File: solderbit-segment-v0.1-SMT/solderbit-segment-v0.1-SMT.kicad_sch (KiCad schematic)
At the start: 13 parts, among them J1 Conn_01x05_Pin, U1 PCF8574AT, U2 PCF8574N

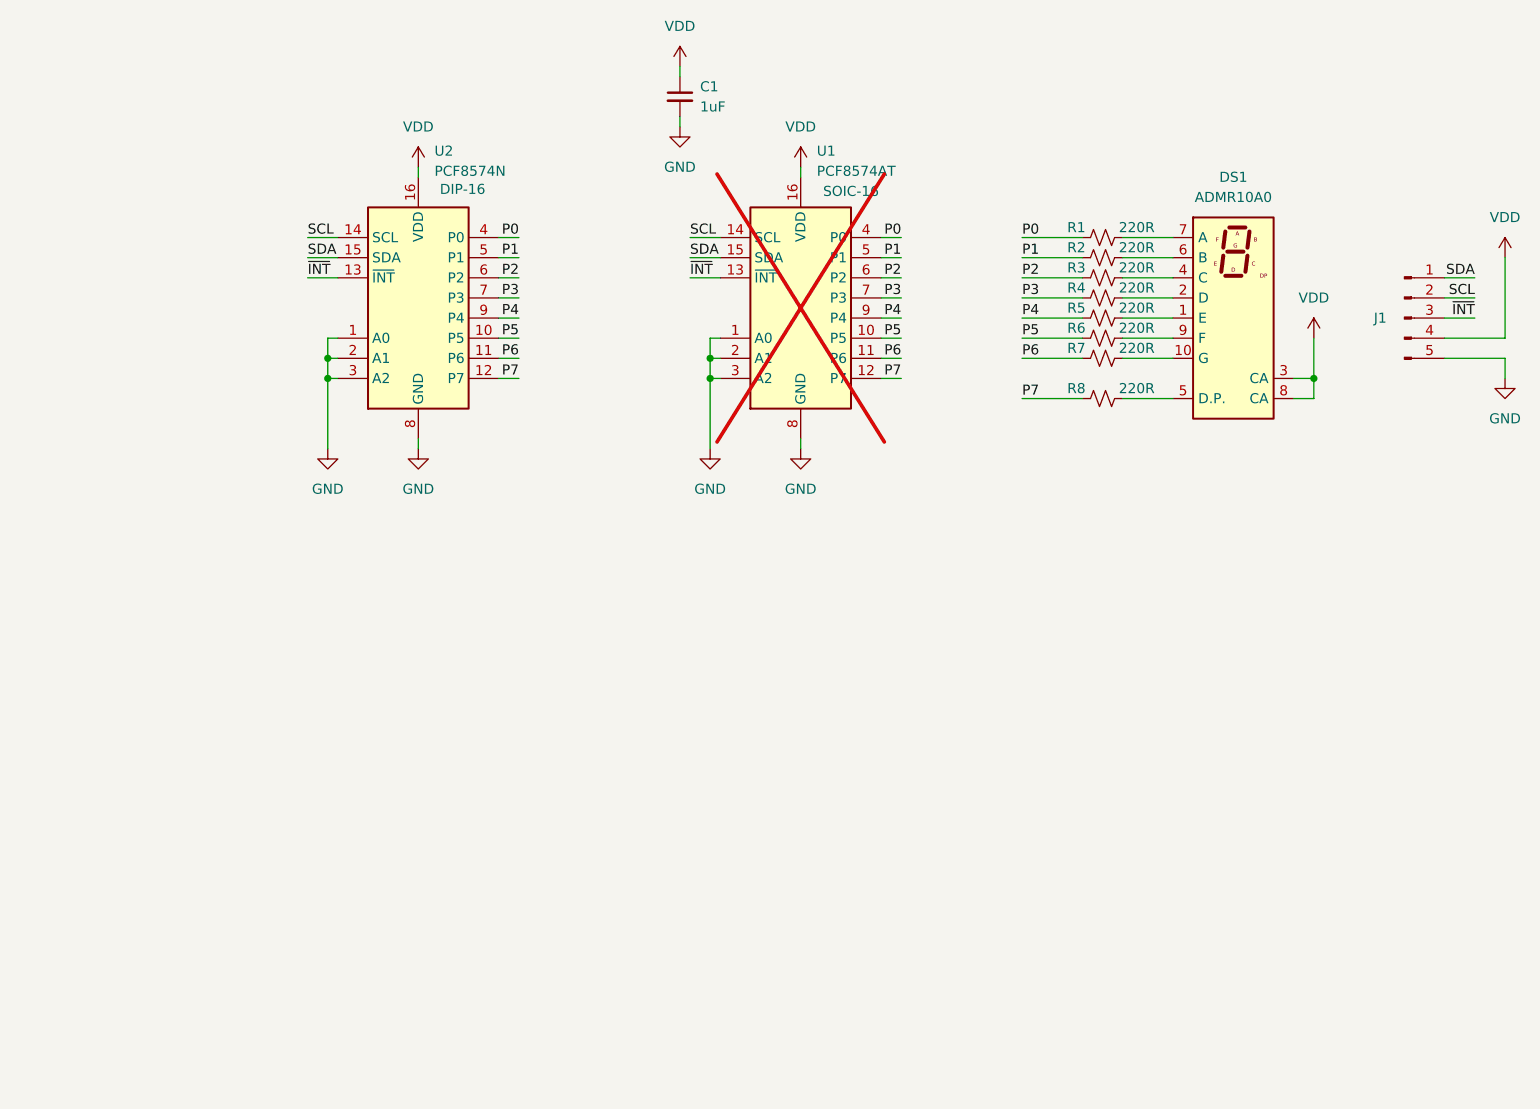
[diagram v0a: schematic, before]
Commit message: Separate SMT version, and THT I/O expander
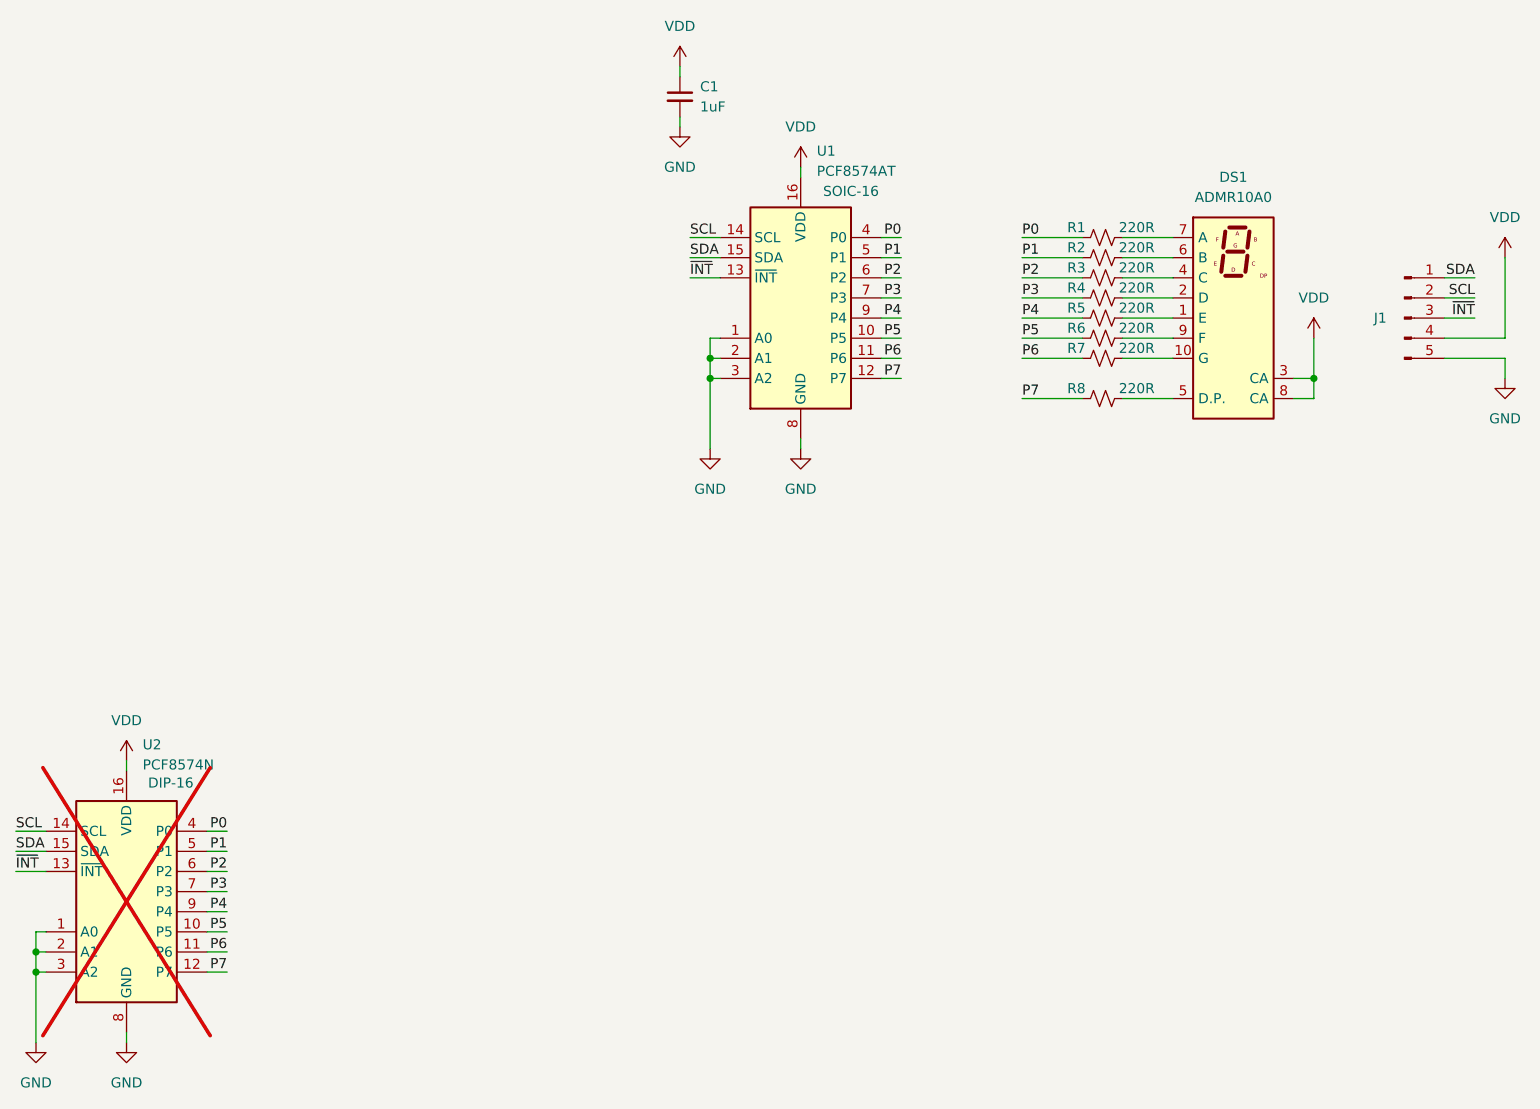
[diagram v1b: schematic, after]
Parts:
- U1: now fitted
- U2: now not fitted
